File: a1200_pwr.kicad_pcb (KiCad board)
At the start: 2 copper layers, 23.2 x 58.2 mm, 20 parts, among them J1 PJ-102A, J2 APWR_big, J3 APWR_small, SW1 RMS1R102M7QES, U1 LMZM23600SILR, U2 RPM5.0-6.0

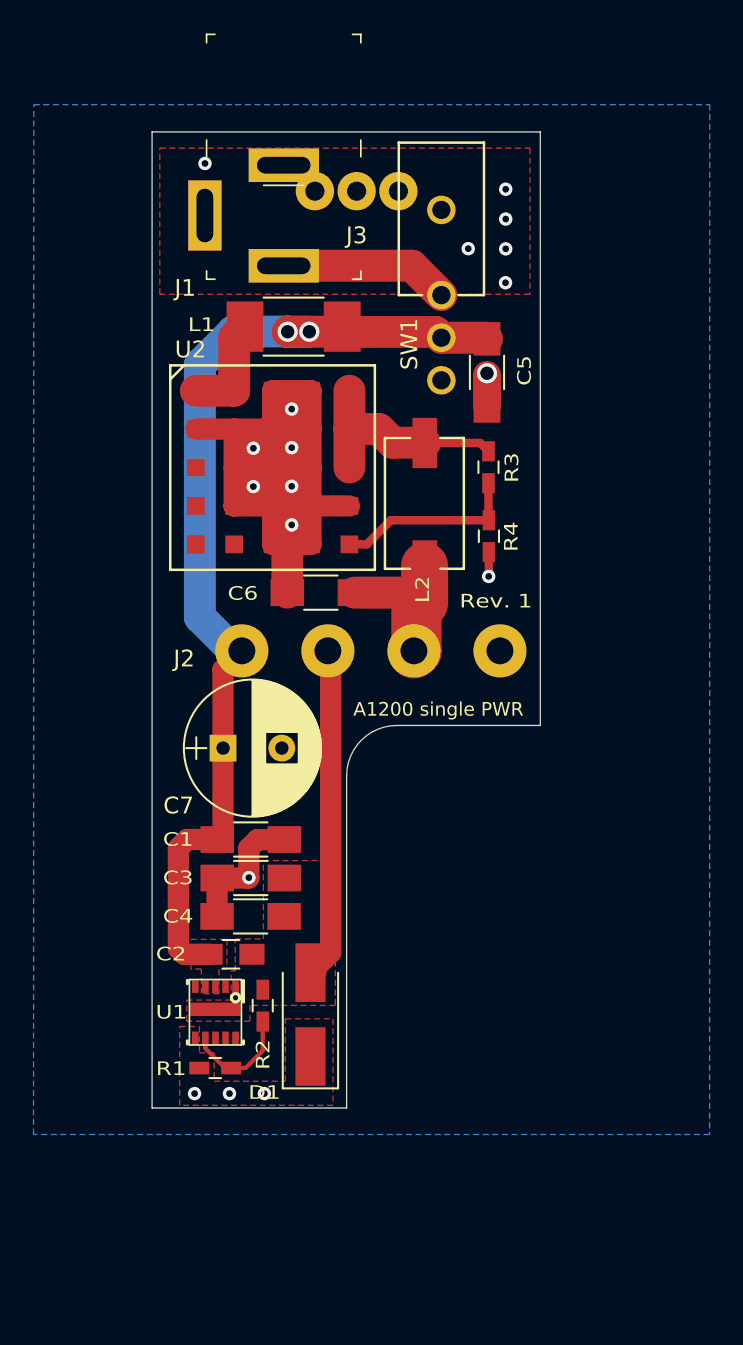
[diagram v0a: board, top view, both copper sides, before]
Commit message: the PGOOD pin of the LMZM23600 was numbered 11 but 5 buy mistake, now the planes are correctly drawn without manual connect of the center pad
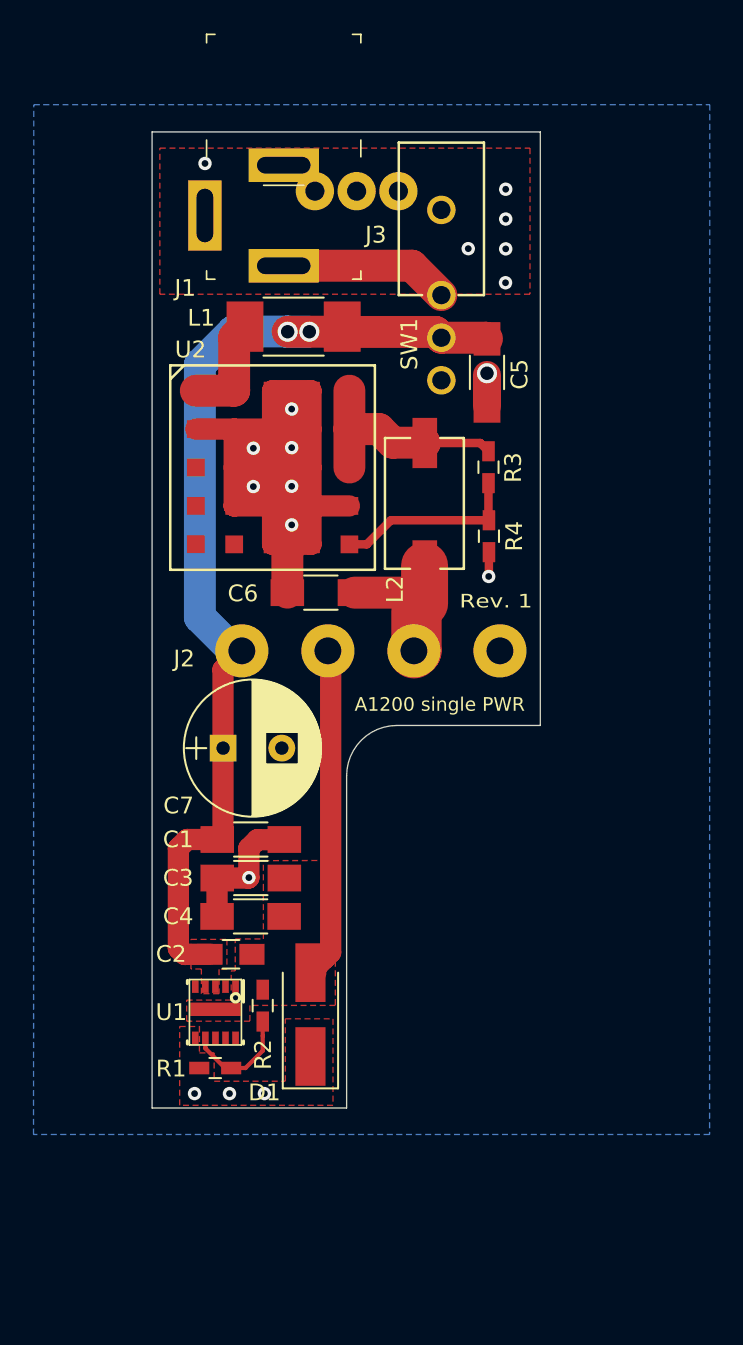
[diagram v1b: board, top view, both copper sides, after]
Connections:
- U1 pad 11: Net-(U1-Pad11) -> -12V
- U1 pad 5: (no net) -> Net-(U1-Pad5)
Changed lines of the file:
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@@
     (mod_text_size 1 1)
     (mod_text_width 0.15)
-    (pad_size 4.2 2)
-    (pad_drill 3.2)
+    (pad_size 0.8 3)
+    (pad_drill 0)
     (pad_to_mask_clearance 0.051)
     (solder_mask_min_width 0.25)
@@
   (net 17 /SW12V)
   (net 18 "Net-(SW1-Pad3)")
-  (net 19 "Net-(U1-Pad11)")
+  (net 19 "Net-(U1-Pad5)")
   (net_class Default "Dies ist die voreingestellte Netzklasse."
     (clearance 0.2)
@@
     (add_net "Net-(SW1-Pad3)")
     (add_net "Net-(U1-Pad10)")
-    (add_net "Net-(U1-Pad11)")
     (add_net "Net-(U1-Pad2)")
+    (add_net "Net-(U1-Pad5)")
     (add_net "Net-(U1-Pad8)")
     (add_net "Net-(U1-Pad9)")
@@
     (at 137.6299 113.0935 270)
     (fp_text reference U1 (at 0 2.6289 180) (layer F.SilkS)
-      (effects (font (size 0.8128 1) (thickness 0.2032)))
+      (effects (font (size 1 1) (thickness 0.15)))
     )
     (fp_text value LMZM23600SILR (at 0 0 90) (layer F.SilkS) hide
@@
       (net 2 +12V) (solder_mask_margin 0.1016))
     (pad 5 smd rect (at -1.525 1.2 270) (size 0.75 0.4) (layers F.Cu F.Paste F.Mask)
-      (solder_mask_margin 0.1016))
+      (net 19 "Net-(U1-Pad5)") (solder_mask_margin 0.1016))
     (pad 6 smd rect (at 1.525 1.2 270) (size 0.75 0.4) (layers F.Cu F.Paste F.Mask)
       (net 1 GND) (solder_mask_margin 0.1016))
@@
       (net 9 "Net-(U1-Pad10)") (solder_mask_margin 0.1016))
     (pad 11 smd rect (at -0.175 0 270) (size 0.8 3) (layers F.Cu F.Paste F.Mask)
-      (net 19 "Net-(U1-Pad11)") (solder_mask_margin 0.1016))
+      (net 3 -12V) (solder_mask_margin 0.1016))
     (model ${KIPRJMOD}/3d/SIL0010A.stp
       (at (xyz 0 0 0))
@@
   (module a1200_pwr:APWR_small (layer F.Cu)
     (at 146.05 64.135)
-    (fp_text reference J3 (at 0 2.643) (layer F.SilkS)
+    (fp_text reference J3 (at 1.143 2.6035) (layer F.SilkS)
       (effects (font (size 1 1) (thickness 0.15)))
     )
@@
   (module a500_pwr:fb_5v (layer F.Cu)
     (at 150.1394 82.7532 90)
-    (fp_text reference L2 (at -5.1308 -0.1524 90) (layer F.SilkS)
-      (effects (font (size 0.8128 1) (thickness 0.2032)))
+    (fp_text reference L2 (at -5.1308 -1.8034 90) (layer F.SilkS)
+      (effects (font (size 1 1) (thickness 0.15)))
     )
     (fp_text value 7427932 (at -3.7 3.6 90) (layer F.Fab)
@@
     (tags "capacitor 1206")
     (attr smd)
-    (fp_text reference C5 (at -0.1143 -2.2352 90) (layer F.SilkS)
-      (effects (font (size 0.8128 1) (thickness 0.2032)))
+    (fp_text reference C5 (at 0.1143 -1.9431 90) (layer F.SilkS)
+      (effects (font (size 1 1) (thickness 0.15)))
     )
     (fp_text value "10u 25V" (at 0 1.75 90) (layer F.Fab)
@@
     (attr smd)
     (fp_text reference C6 (at 4.6482 -0.0508) (layer F.SilkS)
-      (effects (font (size 0.8128 1) (thickness 0.2032)))
+      (effects (font (size 1 1) (thickness 0.15)))
     )
     (fp_text value 22u (at 0 1.75) (layer F.Fab)
@@
     (tags "capacitor 0603")
     (attr smd)
-    (fp_text reference R4 (at -0.0254 1.3335 90) (layer F.SilkS)
-      (effects (font (size 0.8128 1) (thickness 0.2032)))
+    (fp_text reference R4 (at 0 1.5113 90) (layer F.SilkS)
+      (effects (font (size 1 1) (thickness 0.15)))
     )
     (fp_text value Rup (at 0 1.5 90) (layer F.Fab)
@@
     (tags "capacitor 0603")
     (attr smd)
-    (fp_text reference R3 (at -0.0254 1.397 90) (layer F.SilkS)
-      (effects (font (size 0.8128 1) (thickness 0.2032)))
+    (fp_text reference R3 (at -0.0254 1.4732 90) (layer F.SilkS)
+      (effects (font (size 1 1) (thickness 0.15)))
     )
     (fp_text value Rdown (at 0 1.5 90) (layer F.Fab)
@@
     (tags "capacitor 1812")
     (attr smd)
-    (fp_text reference L1 (at -5.4864 -0.1143) (layer F.SilkS)
-      (effects (font (size 0.8128 1) (thickness 0.2032)))
+    (fp_text reference L1 (at -5.5118 -0.5207) (layer F.SilkS)
+      (effects (font (size 1 1) (thickness 0.15)))
     )
     (fp_text value 742792510 (at 0 2.75) (layer F.Fab)
@@
     (attr smd)
     (fp_text reference R2 (at -2.921 0.0254 90) (layer F.SilkS)
-      (effects (font (size 0.8128 1) (thickness 0.2032)))
+      (effects (font (size 1 1) (thickness 0.15)))
     )
     (fp_text value 25.5k (at 0 1.5 90) (layer F.Fab)
@@
     (attr smd)
     (fp_text reference R1 (at -2.6289 0.0381) (layer F.SilkS)
-      (effects (font (size 0.8128 1) (thickness 0.2032)))
+      (effects (font (size 1 1) (thickness 0.15)))
     )
     (fp_text value "280k 1%" (at 0 1.5) (layer F.Fab)
@@
     (attr smd)
     (fp_text reference D1 (at -4.6482 -2.7432) (layer F.SilkS)
-      (effects (font (size 0.8128 1) (thickness 0.2032)))
+      (effects (font (size 1 1) (thickness 0.15)))
     )
     (fp_text value 700mV (at 0 2.6 90) (layer F.Fab)
@@
     (attr smd)
     (fp_text reference C4 (at -4.318 0) (layer F.SilkS)
-      (effects (font (size 0.8128 1) (thickness 0.2032)))
+      (effects (font (size 1 1) (thickness 0.15)))
     )
     (fp_text value 10u (at 0 2) (layer F.Fab)
@@
     (attr smd)
     (fp_text reference C3 (at -4.3307 -0.00635) (layer F.SilkS)
-      (effects (font (size 0.8128 1) (thickness 0.2032)))
+      (effects (font (size 1 1) (thickness 0.15)))
     )
     (fp_text value 10u (at 0 2) (layer F.Fab)
@@
     (attr smd)
     (fp_text reference C2 (at -3.5687 -0.0127) (layer F.SilkS)
-      (effects (font (size 0.8128 1) (thickness 0.2032)))
+      (effects (font (size 1 1) (thickness 0.15)))
     )
     (fp_text value "100n 50V" (at 0 1.75) (layer F.Fab)
@@
     (attr smd)
     (fp_text reference C1 (at -4.3307 0) (layer F.SilkS)
-      (effects (font (size 0.8128 1) (thickness 0.2032)))
+      (effects (font (size 1 1) (thickness 0.15)))
     )
     (fp_text value "10u 25V" (at 0 2) (layer F.Fab)
@@
     (effects (font (size 0.8128 1) (thickness 0.2032)))
   )
-  (gr_text "A1200 single PWR" (at 150.9268 95.0341) (layer F.SilkS)
+  (gr_text "A1200 single PWR" (at 151.003 94.742) (layer F.SilkS)
     (effects (font (size 0.8128 0.8128) (thickness 0.2032)))
   )
@@
   (gr_line (start 133.852 60.6044) (end 157.002 60.6044) (layer Edge.Cuts) (width 0.05))
   (gr_line (start 133.852 118.8044) (end 133.852 60.6044) (layer Edge.Cuts) (width 0.05))
-  (via (at 139.8905 79.4639) (size 0.8) (drill 0.4) (layers F.Cu B.Cu) (net 1) (status 1000000))
+  (via (at 139.8905 79.4639) (size 0.8) (drill 0.4) (layers F.Cu B.Cu) (net 1))
   (via (at 139.8905 81.7499) (size 0.8) (drill 0.4) (layers F.Cu B.Cu) (net 1))
   (via (at 142.1765 81.732966) (size 0.8) (drill 0.4) (layers F.Cu B.Cu) (net 1))

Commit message: Revision 2
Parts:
- C7: footprint Capacitors_THT:CP_Radial_D8.0mm_P3.50mm -> Capacitor_THT:CP_Radial_D6.3mm_P2.50mm
- SW1: value RMS1R102M7QES -> SW_SPDT
- moved C6 23.1 mm to (156.7, 107.3), turned to 0 degrees
- moved U2 21.8 mm to (145.1, 102.1)
- moved L1 21.5 mm to (142.8, 93.7)
- moved J2 19.4 mm to (151.3, 110.4)
- moved J1 19.4 mm to (146.1, 84.4)
- moved R4 19.4 mm to (158.4, 103.6)
- moved SW1 19.4 mm to (155.5, 84.1)
- moved J3 19.4 mm to (150.5, 83.0)
- moved R3 19.4 mm to (158.3, 99.4)
- moved C5 18.6 mm to (143.6, 90.5), turned to 180 degrees
- moved L2 18.5 mm to (154.4, 100.7)
- moved C7 14.4 mm to (151.0, 91.0), turned to -90 degrees
- moved C2 12.0 mm to (142.8, 120.9)
- moved D1 12.0 mm to (147.5, 124.5)
- moved C1 12.0 mm to (144.0, 114.1)
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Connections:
- net Net-(L2-Pad2) renamed /5Vout
- SW1 pad 3: Net-(SW1-Pad3) -> unconnected-(SW1-Pad3)
- U1 pad 10: Net-(U1-Pad10) -> unconnected-(U1-Pad10)
- U1 pad 2: Net-(U1-Pad2) -> unconnected-(U1-Pad2)
- U1 pad 5: Net-(U1-Pad5) -> (no net)
- U1 pad 8: Net-(U1-Pad8) -> unconnected-(U1-Pad8)
- U1 pad 9: Net-(U1-Pad9) -> unconnected-(U1-Pad9)
- U2 pad C1: Net-(U2-PadC1) -> unconnected-(U2-PadC1)
- U2 pad D1: Net-(U2-PadD1) -> unconnected-(U2-PadD1)
- U2 pad E1: Net-(U2-PadE1) -> unconnected-(U2-PadE1)
- U2 pad E2: Net-(U2-PadE2) -> unconnected-(U2-PadE2)
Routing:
- net +12V: track 60.8 -> 52.6 mm, vias 2 -> 1
- net -12V: track 20.6 -> 12.7 mm
- net /5Vout: track 13.4 -> 9.10 mm
- net Net-(R3-Pad1): track 11.1 -> 14.7 mm
- net +5V: track 9.26 -> 5.76 mm
- net GND: track 79.1 -> 80.3 mm, vias 18 -> 20
- added copper zone on F.Cu, net +5V
- added copper zone on F.Cu, net /5Vout
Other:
- board size 23.2 x 58.2 mm -> 23.2 x 50.6 mm
- net class Default removed
- board text added: "Rev. 2"
- board text removed: "Rev. 1"
